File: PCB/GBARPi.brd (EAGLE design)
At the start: 67.3 x 74.3 mm, 55 parts, among them IC1 M68AW128MND, IC2 AD1895, U1 XC3S50ATQ144

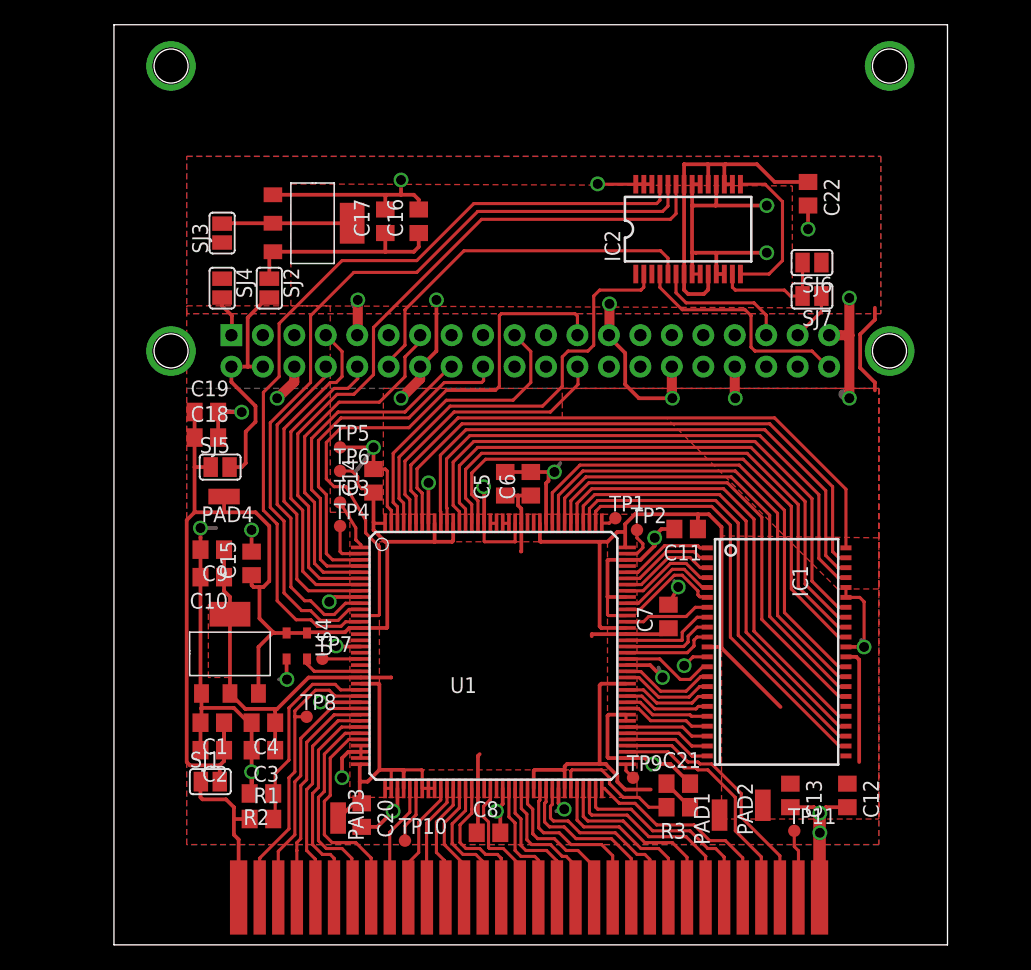
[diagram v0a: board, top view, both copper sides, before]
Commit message: New CM4 version - untested
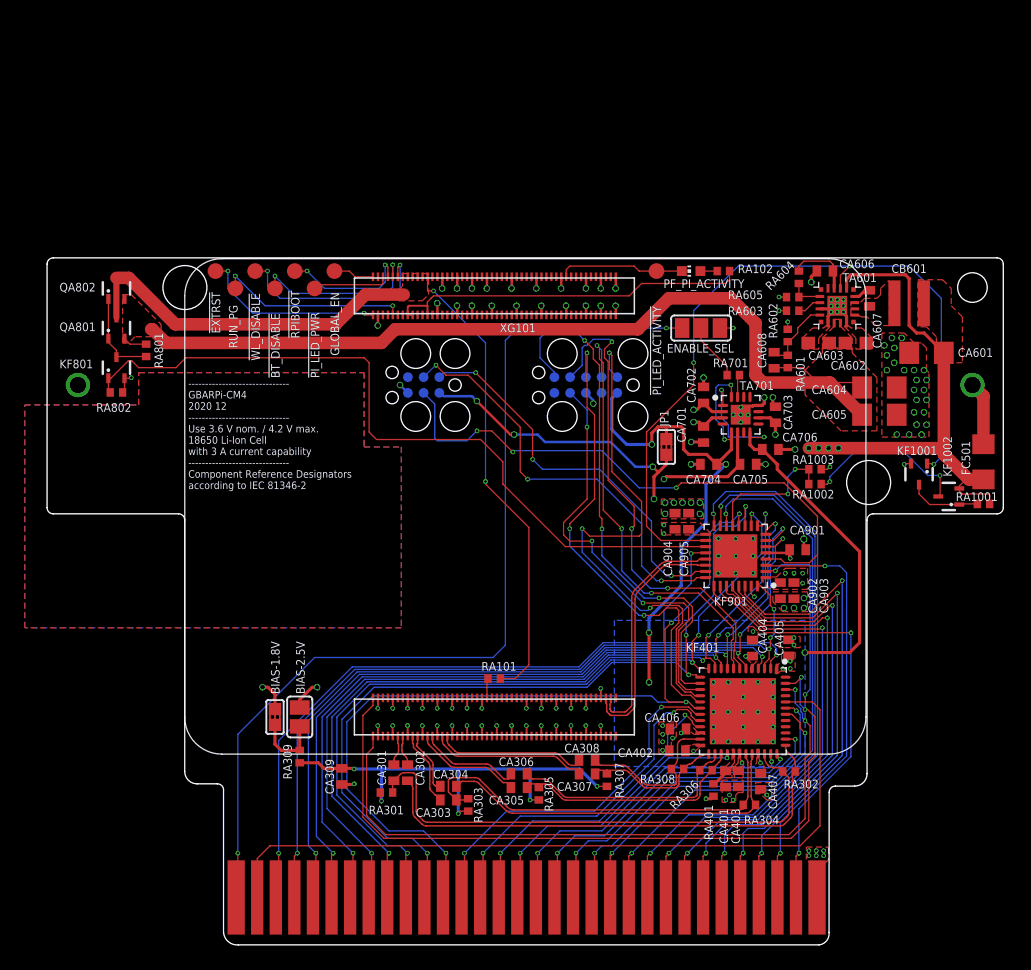
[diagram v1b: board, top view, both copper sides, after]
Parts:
- removed C1, C10, C11, C13, C14, C20, C21, C4, C5, C6, C7, C8: 2u2, rcl:C0805
- removed C12, C15, C16, C18, C19, C2, C22, C3, C9: 10u, rcl:C0805
- removed C17: (no value), rcl:C0805
- removed IC1: M68AW128MND, st-microelectronics:TSOP44-II
- removed IC2: AD1895, AD1895:SSOP28
- removed PAD1, PAD2, PAD3, PAD4: (no value), wirepad:SMD1,27-2,54
- removed R1, R2, R3: (no value), rcl:R0805
- removed SJ1, SJ2, SJ3, SJ4, SJ5, SJ6, SJ7: (no value), jumper:SJ
- removed TP1, TP10, TP11, TP2, TP3, TP4, TP5, TP6, TP7, TP8, TP9: TPTP10R, testpad:TP10R
- removed U$1, U$5: LD1117, LD1117:LD1117SOT-223
- removed U$2: CONNECTOR, gameboy:CONNECTOR
- removed U$3: RPI-ZERO, RPI-Zero:RASPBERRYPI_BASTELSTUBE_V13_RASPI_BOARD_B+_FULL
- removed U$4: ASE, crystal:ASE
- removed U1: XC3S50ATQ144, xilinx_spartan3_virtex4_and_5:TQ144
- added !BT_DISABLE, !EXTRST, !PI_LED_ACTIVITY, !PI_LED_PWR, !RPIBOOT, !WL_DISABLE, GLOBAL_EN, RUN_PG: TPB1,27, testpad:B1,27
- added BIAS-1.8V, JP1: (no value), q:SJS-NC3
- added BIAS-2.5V: (no value), q:SJ
- added CA301, CA302, CA303, CA304, CA305, CA306, CA307, CA308, CA309, CA401, CA402, CA403, CA404, CA405, CA406, CA407, CA606, CA607, CA608, CA701, CA702, CA703, CA704, CA705, CA706, CA901, CA902, CA903, CA904, CA905: (no value), rcl:C0402
- added CA601, CA604, CA605: (no value), rcl:C1206
- added CA602, CA603: (no value), rcl:C0603
- added CB601: 5.6uH, Wurth_Power Magnetics_WE-MAPI:WE-MAPI_4020
- added CC501: 1043, c:BAT_1043
- added ENABLE_SEL: (no value), q:SJ_2
- added FC501: (no value), rcl:R1206
- added KF1001, KF801: BSS138PW, q:SC70-3
- added KF1002, QA801, QA802: NTS2101PT1G, q:SC70-3
- added KF401: ICE40UP5KSG48, c:QFN50P700X700X100-49T535N
- added KF901: STM32F042, c:QFN50P500X500X60-33T350N
- added PF_PI_ACTIVITY: (no value), led:CHIP-LED0603
- added RA1001, RA1002, RA1003, RA102, RA301, RA701, RA801, RA802: 10k, rcl:R0402
- added RA101: 1k, rcl:R0402
- added RA302, RA309: 100, rcl:R0402
- added RA303, RA304, RA305, RA306, RA307, RA308, RA401, RA601, RA602, RA603, RA604, RA605: (no value), rcl:R0402
- added TA601: LT8336, c:LQFN16
- added TA701: ADP322ACPZ-145-R7, c:QFN50P300X300X80-17T175N
- added X1: TC2050, q:TC2050
- added X2: TC2030, q:TC2030
- added XG101: CM4, c:CM4
- added XG201: GBA_CARTRIDGE_CONNECTOR, c:GBA_CARTRIDGE_CONNECTOR
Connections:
- removed net 3V3@2: U$3.17
- removed net AD1895_CLK: IC2.2, U1.P141
- removed net DONE: TP9.TP, U1.P73
- removed net GBA_/CS1: U$2.5, U1.P29
- removed net GBA_/CS2: U$2.30, U1.P76
- removed net GBA_/RD: U$2.4, U1.P28
- removed net GBA_/WR: U$2.3, U1.P27
- removed net GBA_ON: R1.2, R2.1, U1.P24
- removed net I2S_CLK: IC2.5, U$3.12
- removed net I2S_CLK_2: IC2.25, U1.P13
- removed net I2S_DATA: IC2.4, U$3.40
- removed net I2S_DATA_2: IC2.23, U1.P6
- removed net I2S_LRCLK: IC2.6, U$3.35
- removed net I2S_LRCLK_2: IC2.24, U1.P11
- removed net N$13: R3.2, U1.P67
- removed net OSC: U$4.3, U1.P21
- removed net RAM_/CE: IC1.6, U1.P98
- removed net RAM_/OE: IC1.41, U1.P134
- removed net RAM_/WE: IC1.17, U1.P84
- removed net RAM_ADDRESS0: IC1.5, U1.P99
- removed net RAM_ADDRESS1: IC1.4, U1.P101
- removed net RAM_ADDRESS10: IC1.25, U1.P111
- removed net RAM_ADDRESS11: IC1.24, U1.P110
- removed net RAM_ADDRESS12: IC1.22, U1.P77
- removed net RAM_ADDRESS13: IC1.21, U1.P78
- removed net RAM_ADDRESS14: IC1.20, U1.P79
- removed net RAM_ADDRESS15: IC1.19, U1.P82
- removed net RAM_ADDRESS16: IC1.18, U1.P83
- removed net RAM_ADDRESS2: IC1.3, U1.P102
- removed net RAM_ADDRESS3: IC1.2, U1.P103
- removed net RAM_ADDRESS4: IC1.1, U1.P104
- removed net RAM_ADDRESS5: IC1.44, U1.P139
- removed net RAM_ADDRESS6: IC1.43, U1.P138
- removed net RAM_ADDRESS7: IC1.42, U1.P135
- removed net RAM_ADDRESS8: IC1.27, U1.P113
- removed net RAM_ADDRESS9: IC1.26, U1.P112
- removed net RAM_DATA0: IC1.7, U1.P96
- removed net RAM_DATA1: IC1.8, U1.P93
- removed net RAM_DATA10: IC1.31, U1.P116
- removed net RAM_DATA11: IC1.32, U1.P117
- removed net RAM_DATA12: IC1.35, U1.P129
- removed net RAM_DATA13: IC1.36, U1.P130
- removed net RAM_DATA14: IC1.37, U1.P131
- removed net RAM_DATA15: IC1.38, U1.P132
- removed net RAM_DATA2: IC1.9, U1.P92
- removed net RAM_DATA3: IC1.10, U1.P91
- removed net RAM_DATA4: IC1.13, U1.P90
- removed net RAM_DATA5: IC1.14, U1.P88
- removed net RAM_DATA6: IC1.15, U1.P87
- removed net RAM_DATA7: IC1.16, U1.P85
- removed net RAM_DATA8: IC1.29, U1.P114
- removed net RAM_DATA9: IC1.30, U1.P115
- removed net RPI_37: SJ7.1, U$3.37
- removed net RPI_PIN13: U$3.13, U1.P5
- removed net RPI_PIN16: U$3.16, U1.P4
- removed net RPI_PIN18: U$3.18, U1.P3
- removed net RPI_PIN7: U$3.7, U1.P8
- removed net RPI_RXD0: U$3.10, U1.P7
- removed net RPI_TXD0: U$3.8, U1.P10
- removed net SPI0_CS: U$3.24, U1.P140
- removed net SPI0_MISO: U$3.21
- removed net SPI0_MOSI: U$3.19, U1.P142
- removed net SPI0_SCLK: U$3.23, U1.P12
- removed net TCK: TP1.TP, U1.P109
- removed net TDI: TP4.TP, U1.P2
- removed net TDO: TP2.TP, U1.P107
- removed net TMS: TP3.TP, U1.P1
- removed net VCC: C1.1, C11.1, C12.1, C13.1, C14.1, C15.1, C18.1, C19.1, C2.1, C20.1, C21.1, C22.1, IC1.11, IC1.33, IC2.10, IC2.16, IC2.17, IC2.19, IC2.22, IC2.7, PAD1.1, PAD2.1, PAD3.1, PAD4.1, R3.1, SJ1.2, SJ3.1, SJ4.1, SJ5.1, SJ6.1, TP6.TP, U$1.VIN, U$4.1, U$4.4, U1.P108, U1.P119, U1.P133, U1.P136, U1.P14, U1.P144, U1.P23, U1.P36, U1.P37, U1.P38, U1.P40, U1.P43, U1.P44, U1.P45, U1.P61, U1.P66, U1.P86, U1.P95
- removed net VCCINT: C10.1, C3.1, C4.1, C5.1, C6.1, C7.1, C8.1, C9.1, U$1.(VOUT), U$1.VOUT, U1.P122, U1.P22, U1.P52, U1.P94
- new net !BT_DISABLE: !BT_DISABLE.TP, XG101.91
- new net !EXTRST: !EXTRST.TP, XG101.100
- new net !GBA_CS1: KF401.4, XG201.5
- new net !GBA_CS2: KF901.3, XG201.30
- new net !GBA_RD: KF401.3, KF901.32, XG201.4
- new net !GBA_WR: KF401.2, KF901.20, XG201.3
- new net !PI_LED_ACTIVITY: !PI_LED_ACTIVITY.TP, PF_PI_ACTIVITY.C, XG101.21
- new net !PI_LED_PWR: !PI_LED_PWR.TP, XG101.95
- new net !RPIBOOT: !RPIBOOT.TP, XG101.93
- new net !STM_RESET: KF901.4, X2.3
- new net !WL_DISABLE: !WL_DISABLE.TP, XG101.89
- new net +5V_PI: QA801.3, QA802.3, RA101.1, XG101.77, XG101.79, XG101.81, XG101.83, XG101.85, XG101.87
- new net +5V_PI_EN: KF801.1, KF901.19, RA802.2
- new net BAT: CA601.1, CA701.1, CA702.1, CA703.1, CB601.1, ENABLE_SEL.3, FC501.2, KF1002.2, RA1001.2, TA601.13, TA701.10, TA701.2, TA701.3
- new net BATT_VOLTAGE: KF901.13, RA1002.1, RA1003.2
- new net BAT_UNFUSED: CC501.P, FC501.1
- new net CM4_3.3V_OUT: RA102.2, XG101.78, XG101.84, XG101.86
- new net DCDC_EN: KF1001.1, KF901.18, TA601.14
- new net DIFF_BIAS: CA309.1, RA301.2, RA303.2, RA305.2, RA307.2, RA309.2
- new net GLOBAL_EN: GLOBAL_EN.TP, XG101.99
- new net HDMI_CLK_ICE_N: CA301.1, KF401.34, RA301.1, RA302.2
- new net HDMI_CLK_ICE_P: CA302.1, KF401.37, RA302.1
- new net HDMI_CLK_N: CA301.2, XG101.190
- new net HDMI_CLK_P: CA302.2, XG101.188
- new net HDMI_SCL: KF401.46, XG101.200
- new net HDMI_SDA: KF401.47, XG101.199
- new net HDMI_TX0_ICE_N: CA303.1, KF401.31, RA303.1, RA304.2
- new net HDMI_TX0_ICE_P: CA304.1, KF401.32, RA304.1
- new net HDMI_TX0_N: CA303.2, XG101.184
- new net HDMI_TX0_P: CA304.2, XG101.182
- new net HDMI_TX1_ICE_N: CA305.1, KF401.27, RA305.1, RA306.2
- new net HDMI_TX1_ICE_P: CA306.1, KF401.26, RA306.1
- new net HDMI_TX1_N: CA305.2, XG101.178
- new net HDMI_TX1_P: CA306.2, XG101.176
- new net HDMI_TX2_ICE_N: CA307.1, KF401.25, RA307.1, RA308.2
- new net HDMI_TX2_ICE_P: CA308.1, KF401.23, RA308.1
- new net HDMI_TX2_N: CA307.2, XG101.172
- new net HDMI_TX2_P: CA308.2, XG101.170
- new net ICE_CDONE: KF401.7, X1.7
- new net ICE_CRESET_B: KF401.8, X1.9
- new net ICE_SCK: KF401.15, X1.4
- new net ICE_SI: KF401.17, X1.8
- new net ICE_SO: KF401.14, X1.6
- new net ICE_SS: KF401.16, X1.10
- new net ICE_VCC: BIAS-1.8V.1, CA403.1, CA404.1, CA706.1, KF401.30, KF401.5, RA401.2, TA701.1, TA701.8
- new net ICE_VCCIO: CA405.1, CA406.1, CA407.1, CA704.1, JP1.1, KF401.1, KF401.22, KF401.33, TA701.16, TA701.5, X1.1
- new net ICE_VPP_2V5: BIAS-2.5V.1, CA402.1, CA705.1, KF401.24, TA701.6
- new net LT8336_BST: CA607.2, TA601.12
- new net N$1: XG101.151
- new net N$11: BIAS-1.8V.2, BIAS-2.5V.2, RA309.1
- new net N$2: RA101.2, XG101.153
- new net N$3: CA608.2, RA601.1, RA602.2, TA601.4
- new net N$4: CA607.1, CB601.2, TA601.10, TA601.11, TA601.9
- new net N$7: KF801.3, QA801.1, QA802.1, RA801.1
- new net RUN_PG: RUN_PG.TP, XG101.92
- new net STM_SWCLK: KF901.24, X2.4
- new net STM_SWDIO: KF901.23, X2.2
- new net USB_N: KF901.21, XG101.103
- new net USB_P: KF901.22, XG101.105
- new net VCCPLL: CA401.1, KF401.29, RA401.1
- net +3V3: now also CA901.1, CA902.1, CA903.1, CA904.1, CA905.1, JP1.2, KF901.1, KF901.17, KF901.5, X2.1; no longer SJ4.2, U$3.1
- net +5V: now also CA602.1, CA603.1, CA604.1, CA605.1, CA608.1, QA801.2, QA802.2, RA601.2, RA801.2, TA601.6, TA601.7; no longer SJ2.2, SJ5.2, U$3.2, U$3.4
- net GBA_ADDRESS_DATA0: now also KF401.6, KF901.6, XG201.6; no longer U$2.6, U1.P30
- net GBA_ADDRESS_DATA1: now also KF401.9, KF901.7, XG201.7; no longer U$2.7, U1.P31
- net GBA_ADDRESS_DATA10: now also KF401.28, XG201.16; no longer U$2.16, U1.P54
- net GBA_ADDRESS_DATA11: now also KF401.35, XG201.17; no longer U$2.17, U1.P57
- net GBA_ADDRESS_DATA12: now also KF401.36, XG201.18; no longer U$2.18, U1.P58
- net GBA_ADDRESS_DATA13: now also KF401.38, XG201.19; no longer U$2.19, U1.P59
- net GBA_ADDRESS_DATA14: now also KF401.43, XG201.20; no longer U$2.20, U1.P60
- net GBA_ADDRESS_DATA15: now also KF401.42, XG201.21; no longer U$2.21, U1.P62
- net GBA_ADDRESS_DATA16: now also KF901.14, XG201.22; no longer U$2.22, U1.P63
- net GBA_ADDRESS_DATA17: now also KF901.15, XG201.23; no longer U$2.23, U1.P64
- net GBA_ADDRESS_DATA18: now also KF901.16, XG201.24; no longer U$2.24, U1.P68
- net GBA_ADDRESS_DATA19: now also KF901.26, XG201.25; no longer U$2.25, U1.P69
- net GBA_ADDRESS_DATA2: now also KF401.10, KF901.8, XG201.8; no longer U$2.8, U1.P32
- net GBA_ADDRESS_DATA20: now also KF901.27, XG201.26; no longer U$2.26, U1.P70
- net GBA_ADDRESS_DATA21: now also KF901.28, XG201.27; no longer U$2.27, U1.P71
- net GBA_ADDRESS_DATA22: now also KF901.29, XG201.28; no longer U$2.28, U1.P72
- net GBA_ADDRESS_DATA23: now also KF901.30, XG201.29; no longer U$2.29, U1.P75
- net GBA_ADDRESS_DATA3: now also KF401.11, KF901.9, XG201.9; no longer U$2.9, U1.P41
- net GBA_ADDRESS_DATA4: now also KF401.12, KF901.10, XG201.10; no longer U$2.10, U1.P46
- net GBA_ADDRESS_DATA5: now also KF401.13, KF901.11, XG201.11; no longer U$2.11, U1.P47
- net GBA_ADDRESS_DATA6: now also KF401.18, KF901.12, XG201.12; no longer U$2.12, U1.P48
- net GBA_ADDRESS_DATA7: now also KF401.19, XG201.13; no longer U$2.13, U1.P49
- net GBA_ADDRESS_DATA8: now also KF401.20, XG201.14; no longer U$2.14, U1.P50
- net GBA_ADDRESS_DATA9: now also KF401.21, XG201.15; no longer U$2.15, U1.P51
- net GBA_CLK: now also KF401.44, KF901.2, XG201.2; no longer TP8.TP, U$2.2, U1.P25
- net GBA_IRQ: now also KF901.25, XG201.31; no longer TP11.TP, U$2.31
- net GBA_VCC: now also ENABLE_SEL.1, XG201.1; no longer R1.1, SJ1.1, U$2.1
- net GND: now also CA309.2, CA401.2, CA402.2, CA403.2, CA404.2, CA405.2, CA406.2, CA407.2, CA601.2, CA602.2, CA603.2, CA604.2, CA605.2, CA606.2, CA701.2, CA702.2, CA703.2, CA704.2, CA705.2, CA706.2, CA901.2, CA902.2, CA903.2, CA904.2, CA905.2, CC501.N, KF1001.2, KF401.EXP, KF801.2, KF901.31, KF901.33, RA1003.1, RA602.1, RA603.1, RA605.1, RA802.1, TA601.3, TA601.5, TA601.8, TA601.TH, TA701.12, TA701.17, X1.3, X2.5, XG101.1, XG101.107, XG101.108, XG101.113, XG101.114, XG101.119, XG101.120, XG101.125, XG101.126, XG101.13, XG101.131, XG101.132, XG101.137, XG101.138, XG101.14, XG101.144, XG101.150, XG101.155, XG101.156, XG101.161, XG101.162, XG101.167, XG101.168, XG101.173, XG101.174, XG101.179, XG101.180, XG101.185, XG101.186, XG101.191, XG101.192, XG101.197, XG101.198, XG101.2, XG101.22, XG101.23, XG101.32, XG101.33, XG101.42, XG101.43, XG101.52, XG101.53, XG101.59, XG101.60, XG101.65, XG101.66, XG101.7, XG101.71, XG101.74, XG101.8, XG101.98, XG201.32; no longer C1.2, C10.2, C11.2, C12.2, C13.2, C14.2, C15.2, C16.2, C17.2, C18.2, C19.2, C2.2, C20.2, C21.2, C22.2, C3.2, C4.2, C5.2, C6.2, C7.2, C8.2, C9.2, IC1.12, IC1.34, IC1.39, IC1.40, IC2.11, IC2.12, IC2.18, IC2.20, IC2.21, IC2.26, IC2.27, IC2.28, IC2.8, IC2.9, R2.2, TP5.TP, U$1.GND, U$2.32, U$3.14, U$3.25, U$3.30, U$3.34, U$3.39, U$3.6, U$3.9, U$4.2, U$5.GND, U1.P100, U1.P106, U1.P118, U1.P123, U1.P128, U1.P137, U1.P143, U1.P17, U1.P26, U1.P33, U1.P34, U1.P35, U1.P39, U1.P56, U1.P65, U1.P74, U1.P80, U1.P81, U1.P89, U1.P9, U1.P97
- net N$10: now also ENABLE_SEL.2, RA701.1; no longer IC2.14, IC2.15
- net N$12: now also PF_PI_ACTIVITY.A, RA102.1; no longer U1.P124, U1.P125
- net N$14: now also KF1001.3, KF1002.1, RA1001.1; no longer U1.P126, U1.P127
- net N$15: now also KF1002.3, RA1002.2; no longer IC2.13, SJ6.2, SJ7.2
- net N$5: now also RA603.2, TA601.2; no longer SJ3.2, U$5.(VOUT), U$5.VOUT
- net N$6: now also RA604.1, RA605.2, TA601.1; no longer TP7.TP, U1.P19
- net N$8: now also CA606.1, RA604.2, TA601.15; no longer C16.1, C17.1, SJ2.1, U$5.VIN
- net N$9: now also RA701.2, TA701.15; no longer TP10.TP, U1.P42
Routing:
- net VCC: track 241.8 -> 0.00 mm
- net GND: track 248.6 -> 67.0 mm, vias 38 -> 166
- net ICE_VPP_2V5: track 0.00 -> 68.3 mm, vias 0 -> 3
- net ICE_VCC: track 0.00 -> 67.9 mm, vias 0 -> 7
- net !GBA_WR: track 0.00 -> 67.5 mm, vias 0 -> 3
- net I2S_CLK_2: track 67.3 -> 0.00 mm
- net +5V_PI: track 0.00 -> 66.7 mm, vias 0 -> 2
- net I2S_LRCLK_2: track 66.0 -> 0.00 mm
- net GBA_VCC: track 13.0 -> 77.1 mm, vias 0 -> 2
- net DCDC_EN: track 0.00 -> 63.1 mm, vias 0 -> 3
- net !GBA_RD: track 0.00 -> 62.5 mm, vias 0 -> 4
- net BAT: track 0.00 -> 61.3 mm, vias 0 -> 8
- net +5V_PI_EN: track 0.00 -> 61.2 mm
- net HDMI_SDA: track 0.00 -> 61.2 mm, vias 0 -> 2
- net GBA_ADDRESS_DATA6: track 9.64 -> 69.8 mm, vias 0 -> 4
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- added copper zone on layer 1, net +3V3
- added copper zone on layer 15, net +3V3
- added copper zone on layer 1, net +5V
- added copper zone on layer 1, net +5V_PI
- added copper zone on layer 1, net BAT
- added copper zone on layer 15, net BAT
- added copper zone on layer 1, net GND
- added copper zone on layer 15, net GND
- added copper zone on layer 2, net GND
- added copper zone on layer 1, net ICE_VCC
- added copper zone on layer 15, net ICE_VCC
- added copper zone on layer 1, net ICE_VCCIO
- added copper zone on layer 16, net ICE_VCCIO
- added copper zone on layer 1, net ICE_VPP_2V5
- added copper zone on layer 1, net N$4
- added copper zone on layer 1, net VCCPLL
- removed copper zone on layer 1, net N$1
- removed copper zone on layer 1, net N$2
- removed copper zone on layer 1, net VCC
- removed copper zone on layer 1, net VCCINT
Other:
- board size 67.3 x 74.3 mm -> 77.2 x 55.5 mm
- board text added: "------------------------------ GBARPi-CM4 2020 12 ------------------------------ Use 3.6 V nom. / 4.2 V max. 18650 Li-Ion Cell with 3 A current capability ------------------------------ Component Reference Designators according to IEC 81346-2"
